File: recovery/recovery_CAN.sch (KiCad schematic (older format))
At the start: 13 parts

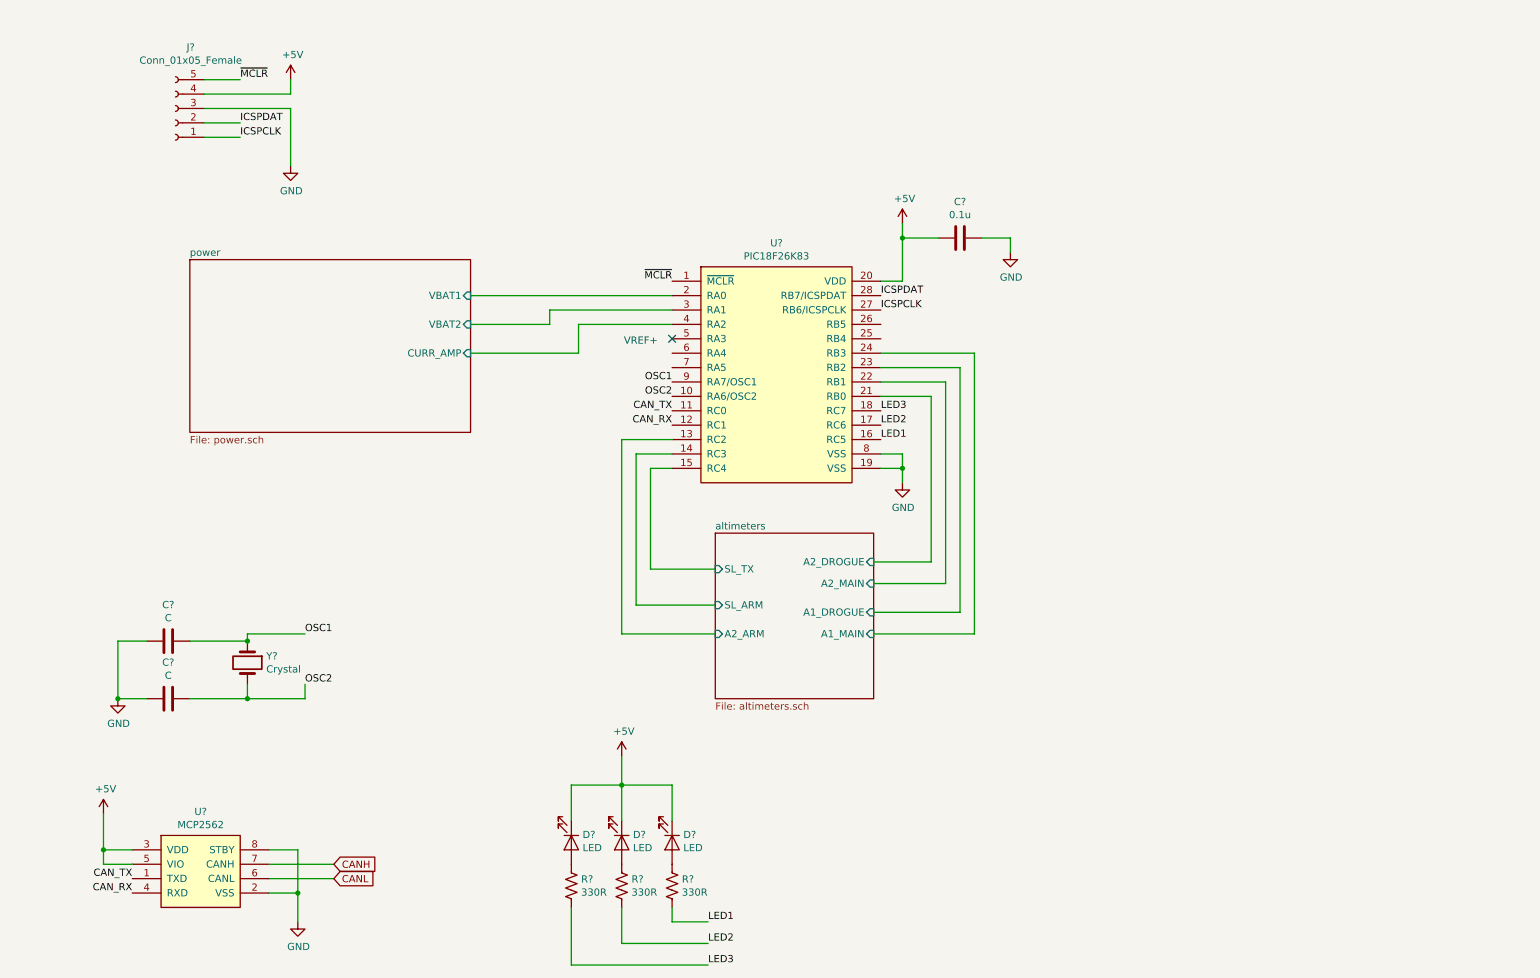
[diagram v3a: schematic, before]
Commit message: Fix level shifting circuit, improve layout of altimiters for better readability, and other small fixes
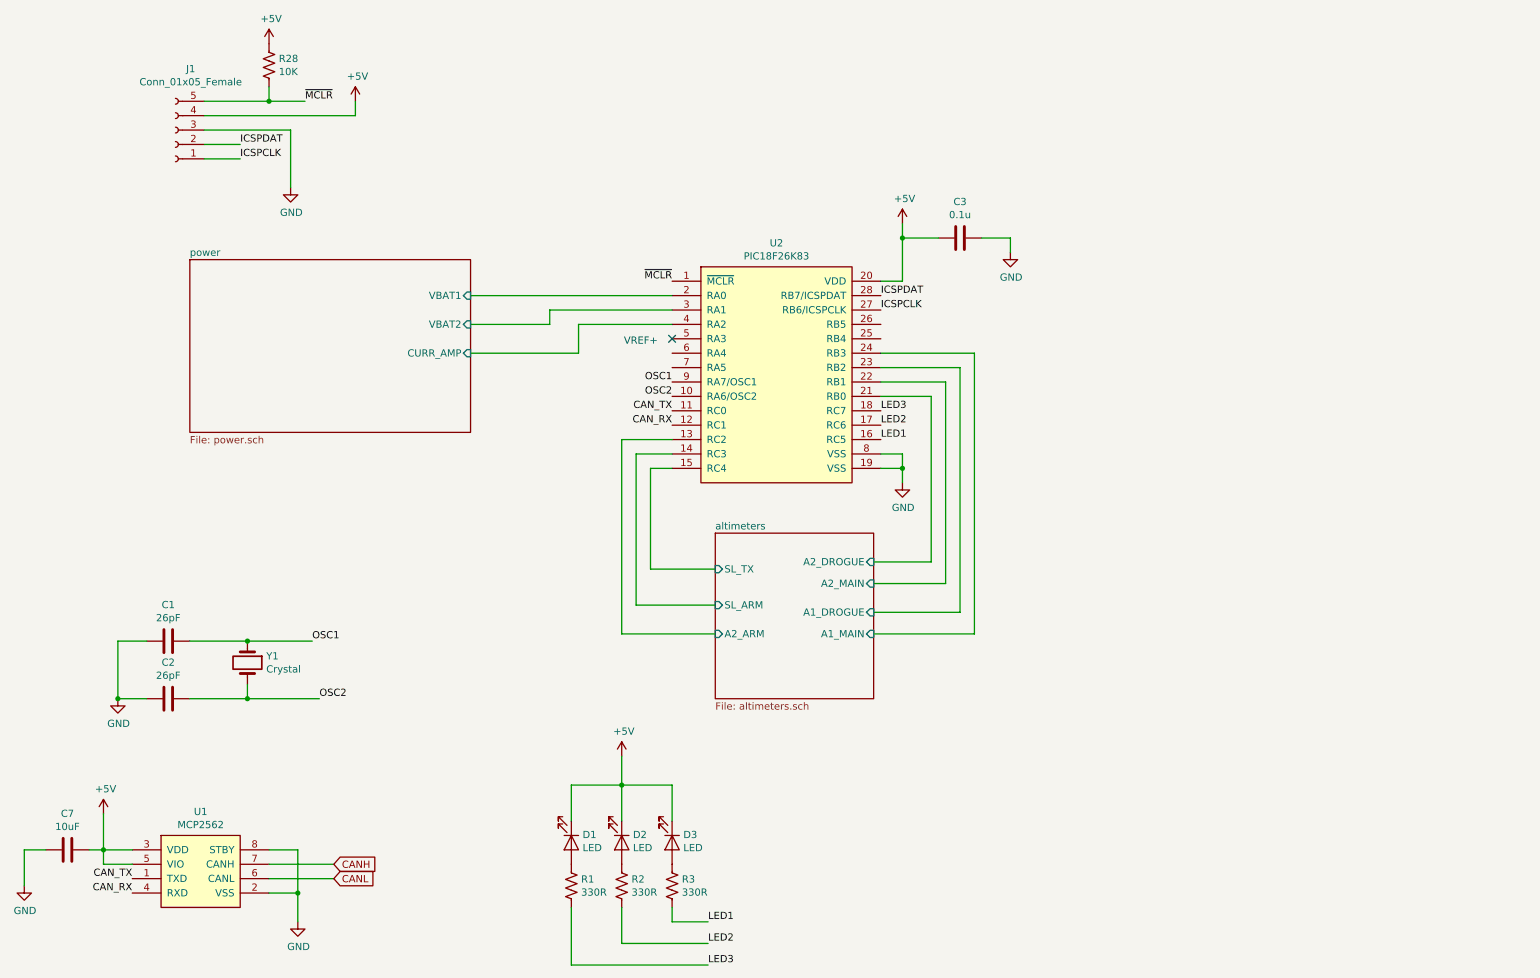
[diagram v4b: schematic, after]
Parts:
- added C7: 10uF, symbol Device:C
- added R28: 10K, symbol Device:R_US
- C1, C2: renamed from C?; value C -> 26pF
- gave numbers to parts that had none: 11
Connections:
- net +5V: now also C7.1, R28.1
- net GND: now also C7.2
- net ~MCLR: now also R28.2
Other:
- moved on the sheet: J1
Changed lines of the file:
@@
 $EndDescr
 $Comp
-L canhw:PIC18F26K83 U?
+L canhw:PIC18F26K83 U2
 U 1 1 5D8FD23F
 P 5900 3150
-F 0 "U?" H 5875 4065 50  0000 C CNN
+F 0 "U2" H 5875 4065 50  0000 C CNN
 F 1 "PIC18F26K83" H 5875 3974 50  0000 C CNN
 F 2 "" H 6350 3150 50  0001 C CNN
@@
 $EndComp
 $Comp
-L Device:C C?
+L Device:C C3
 U 1 1 5D8FD34A
 P 7150 2200
-F 0 "C?" V 6898 2200 50  0000 C CNN
+F 0 "C3" V 6898 2200 50  0000 C CNN
 F 1 "0.1u" V 6989 2200 50  0000 C CNN
 F 2 "" H 7188 2050 50  0001 C CNN
@@
 $EndComp
 $Comp
-L power:+5V #PWR?
+L power:+5V #PWR07
 U 1 1 5D8FD48D
 P 6750 2100
-F 0 "#PWR?" H 6750 1950 50  0001 C CNN
+F 0 "#PWR07" H 6750 1950 50  0001 C CNN
 F 1 "+5V" H 6765 2273 50  0000 C CNN
 F 2 "" H 6750 2100 50  0001 C CNN
@@
 $EndComp
 $Comp
-L power:GND #PWR?
+L power:GND #PWR09
 U 1 1 5D8FD4C8
 P 7500 2300
-F 0 "#PWR?" H 7500 2050 50  0001 C CNN
+F 0 "#PWR09" H 7500 2050 50  0001 C CNN
 F 1 "GND" H 7505 2127 50  0000 C CNN
 F 2 "" H 7500 2300 50  0001 C CNN
@@
 	7500 2200 7500 2300
 $Comp
-L power:GND #PWR?
+L power:GND #PWR08
 U 1 1 5D8FD543
 P 6750 3900
-F 0 "#PWR?" H 6750 3650 50  0001 C CNN
+F 0 "#PWR08" H 6750 3650 50  0001 C CNN
 F 1 "GND" H 6755 3727 50  0000 C CNN
 F 2 "" H 6750 3900 50  0001 C CNN
@@
 Text Label 5150 3300 2    50   ~ 0
 OSC2
-Text Label 2600 4950 0    50   ~ 0
+Text Label 2650 5000 0    50   ~ 0
 OSC1
-Text Label 2600 5300 0    50   ~ 0
+Text Label 2700 5400 0    50   ~ 0
 OSC2
 $Comp
-L Device:Crystal Y?
+L Device:Crystal Y1
 U 1 1 5D8FD67B
 P 2200 5150
-F 0 "Y?" V 2154 5281 50  0000 L CNN
+F 0 "Y1" V 2154 5281 50  0000 L CNN
 F 1 "Crystal" V 2245 5281 50  0000 L CNN
 F 2 "" H 2200 5150 50  0001 C CNN
@@
 $EndComp
 $Comp
-L Device:C C?
+L Device:C C1
 U 1 1 5D8FD6F4
 P 1650 5000
-F 0 "C?" V 1398 5000 50  0000 C CNN
-F 1 "C" V 1489 5000 50  0000 C CNN
+F 0 "C1" V 1398 5000 50  0000 C CNN
+F 1 "26pF" V 1489 5000 50  0000 C CNN
 F 2 "" H 1688 4850 50  0001 C CNN
 F 3 "~" H 1650 5000 50  0001 C CNN
@@
 $EndComp
 $Comp
-L Device:C C?
+L Device:C C2
 U 1 1 5D8FD755
 P 1650 5400
-F 0 "C?" V 1398 5400 50  0000 C CNN
-F 1 "C" V 1489 5400 50  0000 C CNN
+F 0 "C2" V 1398 5400 50  0000 C CNN
+F 1 "26pF" V 1489 5400 50  0000 C CNN
 F 2 "" H 1688 5250 50  0001 C CNN
 F 3 "~" H 1650 5400 50  0001 C CNN
@@
 $EndComp
 $Comp
-L power:GND #PWR?
+L power:GND #PWR02
 U 1 1 5D8FD7A1
 P 1300 5400
-F 0 "#PWR?" H 1300 5150 50  0001 C CNN
+F 0 "#PWR02" H 1300 5150 50  0001 C CNN
 F 1 "GND" H 1305 5227 50  0000 C CNN
 F 2 "" H 1300 5400 50  0001 C CNN
@@
 Wire Wire Line
 	2200 5400 2200 5300
-Wire Wire Line
-	2200 5400 2600 5400
-Wire Wire Line
-	2600 5400 2600 5300
 Connection ~ 2200 5400
-Wire Wire Line
-	2200 5000 2200 4950
-Wire Wire Line
-	2200 4950 2600 4950
-Connection ~ 2200 5000
-$Comp
-L Connector:Conn_01x05_Female J?
+$Comp
+L Connector:Conn_01x05_Female J1
 U 1 1 5D959CC4
-P 1700 1300
-F 0 "J?" H 1594 875 50  0000 C CNN
-F 1 "Conn_01x05_Female" H 1594 966 50  0000 C CNN
-F 2 "" H 1700 1300 50  0001 C CNN
-F 3 "~" H 1700 1300 50  0001 C CNN
-	1    1700 1300
+P 1700 1450
+F 0 "J1" H 1594 1025 50  0000 C CNN
+F 1 "Conn_01x05_Female" H 1594 1116 50  0000 C CNN
+F 2 "" H 1700 1450 50  0001 C CNN
+F 3 "~" H 1700 1450 50  0001 C CNN
+	1    1700 1450
 	-1   0    0    1
 $EndComp
-Text Label 2150 1100 0    50   ~ 0
+Text Label 2600 1250 0    50   ~ 0
 ~MCLR
 Wire Wire Line
-	1900 1100 2150 1100
-$Comp
-L power:+5V #PWR?
+	1900 1250 2350 1250
+$Comp
+L power:+5V #PWR03
 U 1 1 5D95A01E
-P 2500 1100
-F 0 "#PWR?" H 2500 950 50  0001 C CNN
-F 1 "+5V" H 2515 1273 50  0000 C CNN
-F 2 "" H 2500 1100 50  0001 C CNN
-F 3 "" H 2500 1100 50  0001 C CNN
-	1    2500 1100
-	1    0    0    -1
-$EndComp
-Wire Wire Line
-	1900 1200 2500 1200
-Wire Wire Line
-	2500 1200 2500 1100
-$Comp
-L power:GND #PWR?
+P 2950 1250
+F 0 "#PWR03" H 2950 1100 50  0001 C CNN
+F 1 "+5V" H 2965 1423 50  0000 C CNN
+F 2 "" H 2950 1250 50  0001 C CNN
+F 3 "" H 2950 1250 50  0001 C CNN
+	1    2950 1250
+	1    0    0    -1
+$EndComp
+Wire Wire Line
+	1900 1350 2950 1350
+Wire Wire Line
+	2950 1350 2950 1250
+$Comp
+L power:GND #PWR04
 U 1 1 5D95A4EB
-P 2500 1700
-F 0 "#PWR?" H 2500 1450 50  0001 C CNN
-F 1 "GND" H 2505 1527 50  0000 C CNN
-F 2 "" H 2500 1700 50  0001 C CNN
-F 3 "" H 2500 1700 50  0001 C CNN
-	1    2500 1700
-	1    0    0    -1
-$EndComp
-Wire Wire Line
-	1900 1300 2500 1300
-Wire Wire Line
-	2500 1300 2500 1700
-Text Label 2150 1500 0    50   ~ 0
+P 2500 1850
+F 0 "#PWR04" H 2500 1600 50  0001 C CNN
+F 1 "GND" H 2505 1677 50  0000 C CNN
+F 2 "" H 2500 1850 50  0001 C CNN
+F 3 "" H 2500 1850 50  0001 C CNN
+	1    2500 1850
+	1    0    0    -1
+$EndComp
+Wire Wire Line
+	1900 1450 2500 1450
+Wire Wire Line
+	2500 1450 2500 1850
+Text Label 2150 1650 0    50   ~ 0
 ICSPCLK
-Text Label 2150 1400 0    50   ~ 0
+Text Label 2150 1550 0    50   ~ 0
 ICSPDAT
 Wire Wire Line
-	2150 1400 1900 1400
-Wire Wire Line
-	2150 1500 1900 1500
+	2150 1550 1900 1550
+Wire Wire Line
+	2150 1650 1900 1650
 Text Label 6600 2600 0    50   ~ 0
 ICSPDAT
@@
 $EndSheet
 $Comp
-L Device:LED D?
+L Device:LED D3
 U 1 1 5DAA8959
 P 5150 6400
-F 0 "D?" V 5095 6478 50  0000 L CNN
+F 0 "D3" V 5095 6478 50  0000 L CNN
 F 1 "LED" V 5186 6478 50  0000 L CNN
 F 2 "" H 5150 6400 50  0001 C CNN
@@
 $EndComp
 $Comp
-L Device:LED D?
+L Device:LED D2
 U 1 1 5DAA89D1
 P 4800 6400
-F 0 "D?" V 4745 6478 50  0000 L CNN
+F 0 "D2" V 4745 6478 50  0000 L CNN
 F 1 "LED" V 4836 6478 50  0000 L CNN
 F 2 "" H 4800 6400 50  0001 C CNN
@@
 $EndComp
 $Comp
-L Device:LED D?
+L Device:LED D1
 U 1 1 5DAA8A2E
 P 4450 6400
-F 0 "D?" V 4395 6478 50  0000 L CNN
+F 0 "D1" V 4395 6478 50  0000 L CNN
 F 1 "LED" V 4486 6478 50  0000 L CNN
 F 2 "" H 4450 6400 50  0001 C CNN
@@
 $EndComp
 $Comp
-L power:+5V #PWR?
+L power:+5V #PWR06
 U 1 1 5DAA8A9F
 P 4800 5800
-F 0 "#PWR?" H 4800 5650 50  0001 C CNN
+F 0 "#PWR06" H 4800 5650 50  0001 C CNN
 F 1 "+5V" H 4815 5973 50  0000 C CNN
 F 2 "" H 4800 5800 50  0001 C CNN
@@
 	4800 6000 4800 5800
 $Comp
-L Device:R_US R?
+L Device:R_US R3
 U 1 1 5DAA98F4
 P 5150 6700
-F 0 "R?" H 5218 6746 50  0000 L CNN
+F 0 "R3" H 5218 6746 50  0000 L CNN
 F 1 "330R" H 5218 6655 50  0000 L CNN
 F 2 "" V 5190 6690 50  0001 C CNN
@@
 $EndComp
 $Comp
-L Device:R_US R?
+L Device:R_US R2
 U 1 1 5DAA9942
 P 4800 6700
-F 0 "R?" H 4868 6746 50  0000 L CNN
+F 0 "R2" H 4868 6746 50  0000 L CNN
 F 1 "330R" H 4868 6655 50  0000 L CNN
 F 2 "" V 4840 6690 50  0001 C CNN
@@
 $EndComp
 $Comp
-L Device:R_US R?
+L Device:R_US R1
 U 1 1 5DAA9AA5
 P 4450 6700
-F 0 "R?" H 4518 6746 50  0000 L CNN
+F 0 "R1" H 4518 6746 50  0000 L CNN
 F 1 "330R" H 4518 6655 50  0000 L CNN
 F 2 "" V 4490 6690 50  0001 C CNN
@@
 $EndComp
 $Comp
-L canhw:MCP2562 U?
+L canhw:MCP2562 U1
 U 1 1 5DAA9FEB
 P 1900 6450
-F 0 "U?" H 1875 6715 50  0000 C CNN
+F 0 "U1" H 1875 6715 50  0000 C CNN
 F 1 "MCP2562" H 1875 6624 50  0000 C CNN
 F 2 "" H 1900 6450 50  0001 C CNN
@@
 $EndComp
 $Comp
-L power:+5V #PWR?
+L power:+5V #PWR01
 U 1 1 5DAAA5AA
 P 1200 6200
-F 0 "#PWR?" H 1200 6050 50  0001 C CNN
+F 0 "#PWR01" H 1200 6050 50  0001 C CNN
 F 1 "+5V" H 1215 6373 50  0000 C CNN
 F 2 "" H 1200 6200 50  0001 C CNN
@@
 $EndComp
 $Comp
-L power:GND #PWR?
+L power:GND #PWR05
 U 1 1 5DAAA7CF
 P 2550 6950
-F 0 "#PWR?" H 2550 6700 50  0001 C CNN
+F 0 "#PWR05" H 2550 6700 50  0001 C CNN
 F 1 "GND" H 2555 6777 50  0000 C CNN
 F 2 "" H 2550 6950 50  0001 C CNN
@@
 Wire Wire Line
 	7250 3000 6600 3000
+$Comp
+L Device:R_US R28
+U 1 1 5DBB3301
+P 2350 1000
+F 0 "R28" H 2418 1046 50  0000 L CNN
+F 1 "10K" H 2418 955 50  0000 L CNN
+F 2 "" V 2390 990 50  0001 C CNN
+F 3 "~" H 2350 1000 50  0001 C CNN
+	1    2350 1000
+	1    0    0    -1
+$EndComp
+$Comp
+L power:+5V #PWR050
+U 1 1 5DBB3354
+P 2350 850
+F 0 "#PWR050" H 2350 700 50  0001 C CNN
+F 1 "+5V" H 2365 1023 50  0000 C CNN
+F 2 "" H 2350 850 50  0001 C CNN
+F 3 "" H 2350 850 50  0001 C CNN
+	1    2350 850
+	1    0    0    -1
+$EndComp
+Wire Wire Line
+	2350 1150 2350 1250
+Connection ~ 2350 1250
+Wire Wire Line
+	2350 1250 2600 1250
+$Comp
+L Device:C C7
+U 1 1 5DBBA512
+P 950 6450
+F 0 "C7" V 698 6450 50  0000 C CNN
+F 1 "10uF" V 789 6450 50  0000 C CNN
+F 2 "" H 988 6300 50  0001 C CNN
+F 3 "~" H 950 6450 50  0001 C CNN
+	1    950  6450
+	0    1    1    0
+$EndComp
+Wire Wire Line
+	1200 6450 1100 6450
+$Comp
+L power:GND #PWR023
+U 1 1 5DBBD9EB
+P 650 6700
+F 0 "#PWR023" H 650 6450 50  0001 C CNN
+F 1 "GND" H 655 6527 50  0000 C CNN
+F 2 "" H 650 6700 50  0001 C CNN
+F 3 "" H 650 6700 50  0001 C CNN
+	1    650  6700
+	1    0    0    -1
+$EndComp
+Wire Wire Line
+	650  6700 650  6450
+Wire Wire Line
+	650  6450 800  6450
+Wire Wire Line
+	2200 5400 2700 5400
+Wire Wire Line
+	2200 5000 2650 5000
+Connection ~ 2200 5000
 $EndSCHEMATC

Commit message: fix minor comments
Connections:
- net +5V: now also D1.2 (A), D2.2 (A), D3.2 (A); no longer D1.1 (K), D2.1 (K), D3.1 (K)
- net at R3.1: now also D3.1 (K); no longer D3.2 (A)
- net at R2.1: now also D2.1 (K); no longer D2.2 (A)
- net at R1.1: now also D1.1 (K); no longer D1.2 (A)
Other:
- moved on the sheet: D1, D2, D3
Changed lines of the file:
@@
 F 3 "~" H 5150 6400 50  0001 C CNN
 	1    5150 6400
-	0    1    1    0
+	0    -1   -1   0
 $EndComp
 $Comp
@@
 F 3 "~" H 4800 6400 50  0001 C CNN
 	1    4800 6400
-	0    1    1    0
+	0    -1   -1   0
 $EndComp
 $Comp
@@
 F 3 "~" H 4450 6400 50  0001 C CNN
 	1    4450 6400
-	0    1    1    0
+	0    -1   -1   0
 $EndComp
 $Comp
